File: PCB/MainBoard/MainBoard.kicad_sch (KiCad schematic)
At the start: 18 parts, among them J10 Conn_01x06_Socket, J11 Conn_01x06_Socket, J12 Conn_01x04_Socket, J18 Conn_01x04_Socket, J19 Conn_01x04_Socket, J20 Conn_01x04_Socket, J5 Conn_01x03_Socket, J6 Conn_01x03_Socket, J7 Conn_01x03_Socket, SW1 SW_Push, U3 STM32F103C8Tx

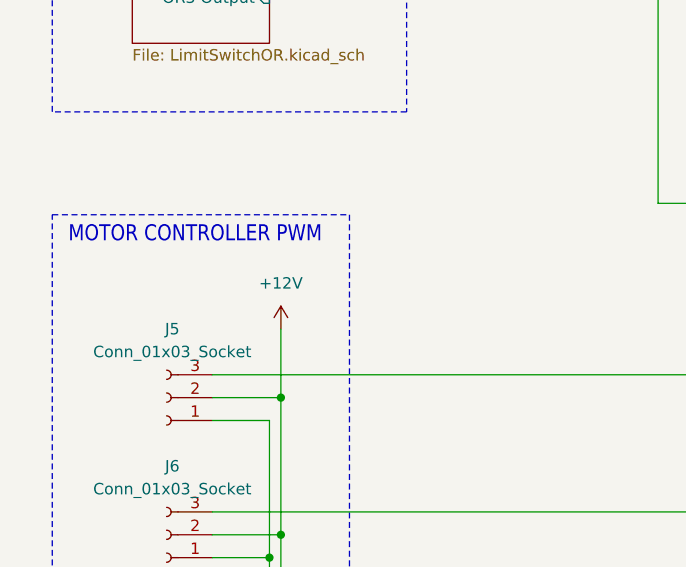
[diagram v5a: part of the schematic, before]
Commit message: final layout v1 - unconnected
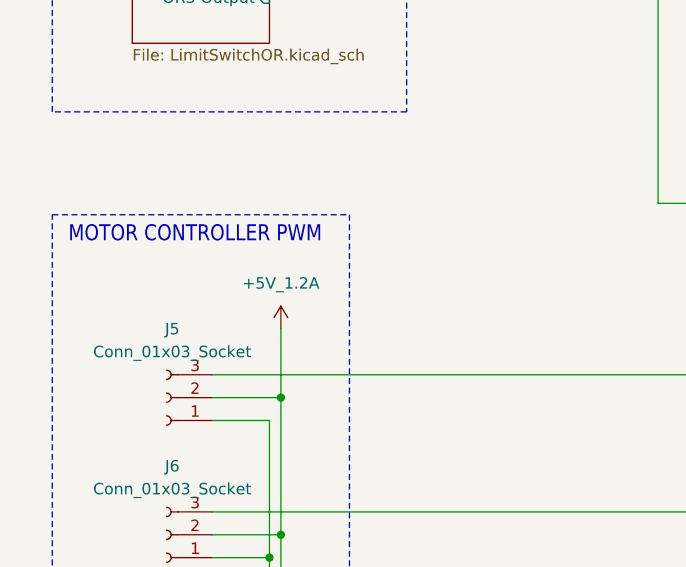
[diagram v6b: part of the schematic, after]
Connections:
- net +12V: no longer J5.2 (Pin_2), J6.2 (Pin_2), J7.2 (Pin_2)
- net +5V_1.2A: now also J5.2 (Pin_2), J6.2 (Pin_2), J7.2 (Pin_2)
